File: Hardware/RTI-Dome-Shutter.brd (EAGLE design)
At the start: 80 x 71.1 mm, 42 parts, among them IC1 24AA128ST, IC5 74LVC245, IC6 74ABT245, J1 POWERPOLE_POWER45A

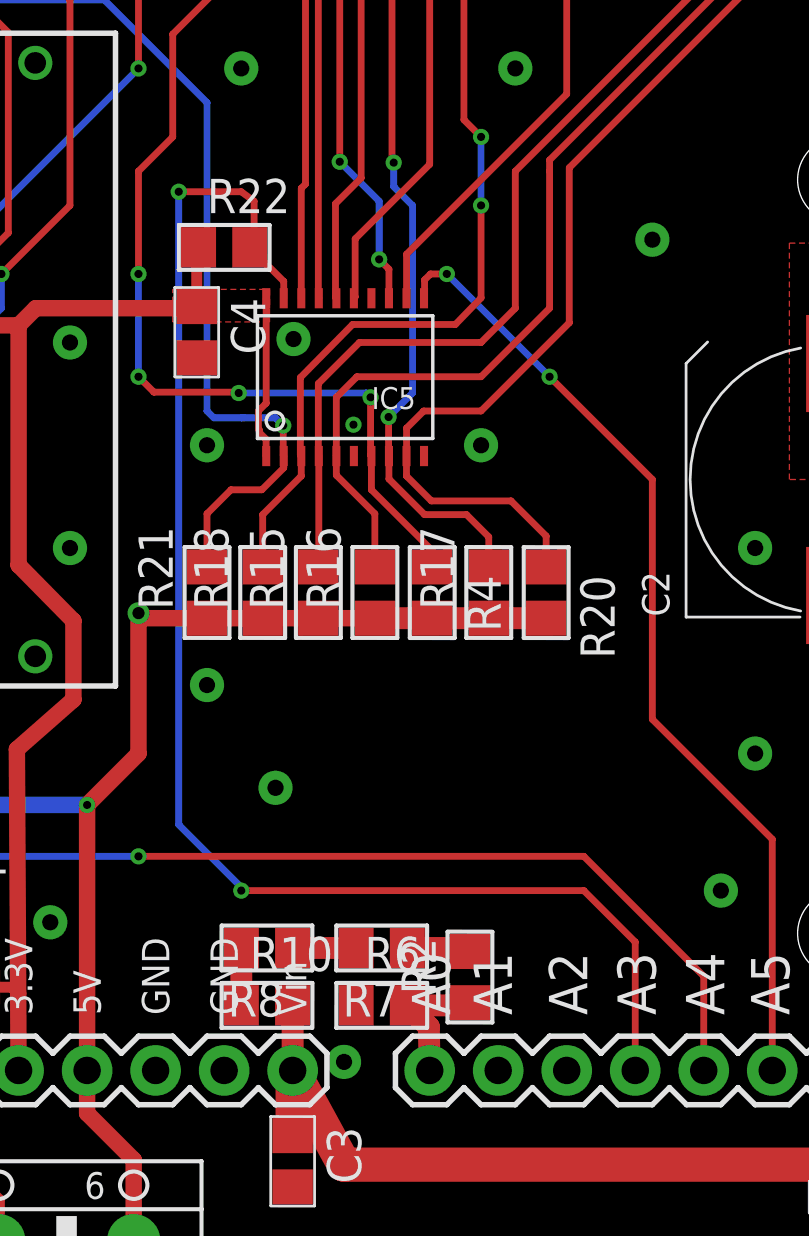
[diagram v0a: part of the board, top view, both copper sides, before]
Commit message: Added FTDI reset as it wasn't doing a proper reset on power up. Finished IP config in the plugin.
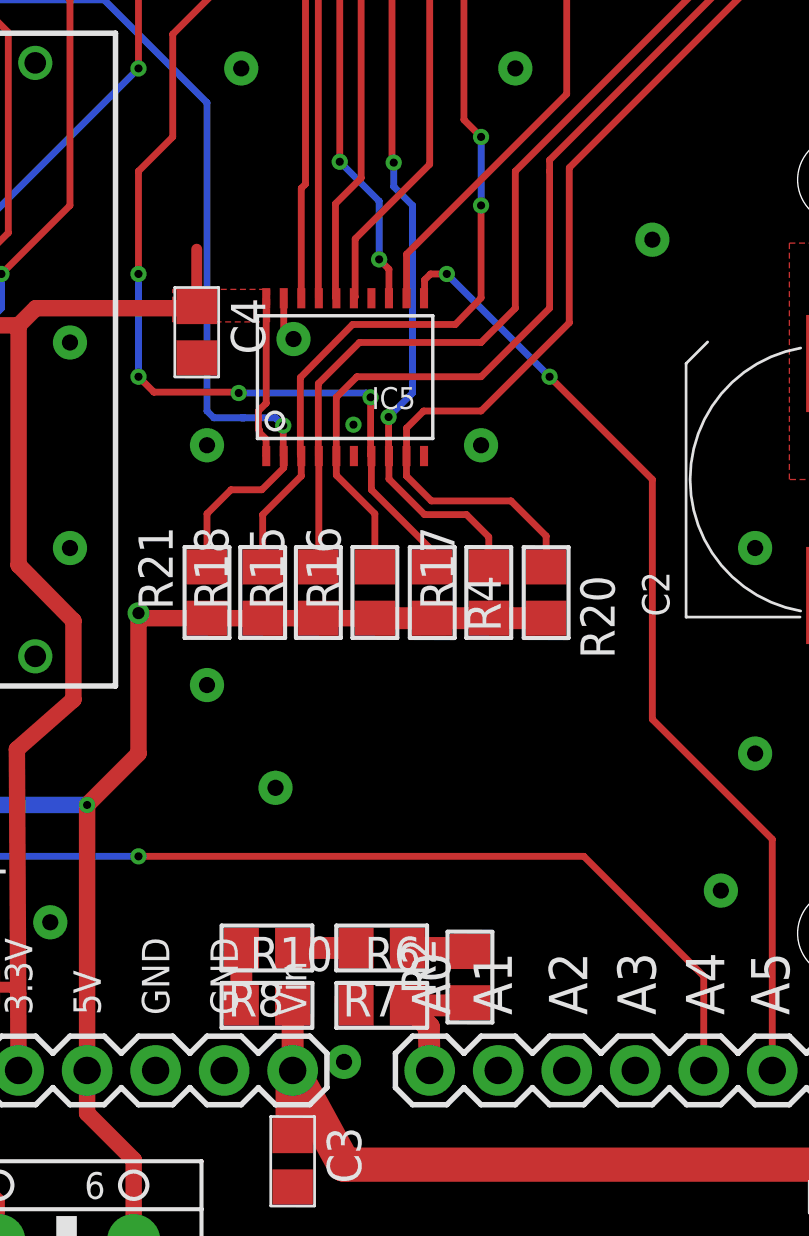
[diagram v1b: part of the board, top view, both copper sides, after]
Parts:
- removed R22: 4.7K, rti:R0805
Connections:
- removed net BUF_EN: IC5.P$19, PCB1.A3, R22.2
- net 3.3V: no longer R22.1
- net GND: now also IC5.P$19
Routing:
- net BUF_EN: track 54.1 -> 0.00 mm, vias 2 -> 0
- net GND: track 0.00 -> 1.66 mm
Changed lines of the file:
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@@
 <element name="IC5" library="rti" package="TSSOP20" value="74LVC245" x="36.83" y="36.83" rot="R90"/>
 <element name="IC6" library="rti" package="TSSOP20" value="74ABT245" x="11.43" y="19.05" rot="R180"/>
-<element name="R22" library="rti" package="R0805" value="4.7K" x="32.385" y="41.62425"/>
 <element name="J1" library="powerpoles" package="POWERPOLE_PAIR_45A" value="POWERPOLE_POWER45A" x="63.5" y="33.02" rot="R270"/>
 <element name="U$1" library="MCP120T-270I_TT" package="SOT95P237X112-3N" value="MCP120T-270I_TT" x="22.86" y="15.24">
@@
 <contactref element="J1" pad="BLACK"/>
 <contactref element="U$1" pad="3"/>
+<contactref element="IC5" pad="P$19"/>
+<wire x1="34.595" y1="39.74" x2="34.595" y2="38.58875" width="0.254" layer="1"/>
+<wire x1="34.595" y1="38.58875" x2="34.95675" y2="38.227" width="0.254" layer="1"/>
 </signal>
 <signal name="+12V" class="1">
@@
 <contactref element="IC5" pad="P$20"/>
 <contactref element="IC5" pad="P$1"/>
-<contactref element="R22" pad="1"/>
 <wire x1="33.945" y1="33.89" x2="33.94075" y2="33.89425" width="0.254" layer="1"/>
 <wire x1="33.94075" y1="33.89425" x2="33.94075" y2="34.51225" width="0.254" layer="1"/>
@@
 <wire x1="33.655" y1="35.56" x2="33.945" y2="35.85" width="0.254" layer="1"/>
 <wire x1="33.945" y1="35.85" x2="33.945" y2="39.74" width="0.254" layer="1"/>
-<wire x1="31.435" y1="41.62425" x2="31.369" y2="41.55825" width="0.4064" layer="1"/>
 <wire x1="31.369" y1="41.55825" x2="31.369" y2="39.431" width="0.4064" layer="1"/>
 <contactref element="U$1" pad="2"/>
@@
 <wire x1="3.8354" y1="63.4746" x2="5.08" y2="62.23" width="0.254" layer="1"/>
 </signal>
-<signal name="BUF_EN">
-<contactref element="IC5" pad="P$19"/>
-<contactref element="R22" pad="2"/>
-<wire x1="34.595" y1="39.74" x2="34.595" y2="40.36425" width="0.254" layer="1"/>
-<wire x1="34.595" y1="40.36425" x2="33.335" y2="41.62425" width="0.254" layer="1"/>
-<contactref element="PCB1" pad="A3"/>
-<wire x1="47.625" y1="11.1125" x2="47.625" y2="15.875" width="0.254" layer="1"/>
-<wire x1="47.625" y1="15.875" x2="45.72" y2="17.78" width="0.254" layer="1"/>
-<wire x1="45.72" y1="17.78" x2="33.02" y2="17.78" width="0.254" layer="1"/>
-<via x="33.02" y="17.78" extent="1-16" drill="0.3" diameter="0.254"/>
-<wire x1="33.02" y1="17.78" x2="33.02" y2="17.907" width="0.254" layer="16"/>
-<wire x1="33.02" y1="17.907" x2="30.70225" y2="20.22475" width="0.254" layer="16"/>
-<wire x1="30.70225" y1="20.22475" x2="30.70225" y2="43.688" width="0.254" layer="16"/>
-<via x="30.70225" y="43.688" extent="1-16" drill="0.3" diameter="0.254"/>
-<wire x1="30.70225" y1="43.688" x2="33.02" y2="43.688" width="0.254" layer="1"/>
-<wire x1="33.02" y1="43.688" x2="33.49625" y2="43.33875" width="0.254" layer="1"/>
-<wire x1="33.49625" y1="43.33875" x2="33.49625" y2="41.7855" width="0.254" layer="1"/>
-<wire x1="33.49625" y1="41.7855" x2="33.335" y2="41.62425" width="0.254" layer="1"/>
-</signal>
 <signal name="N$4">

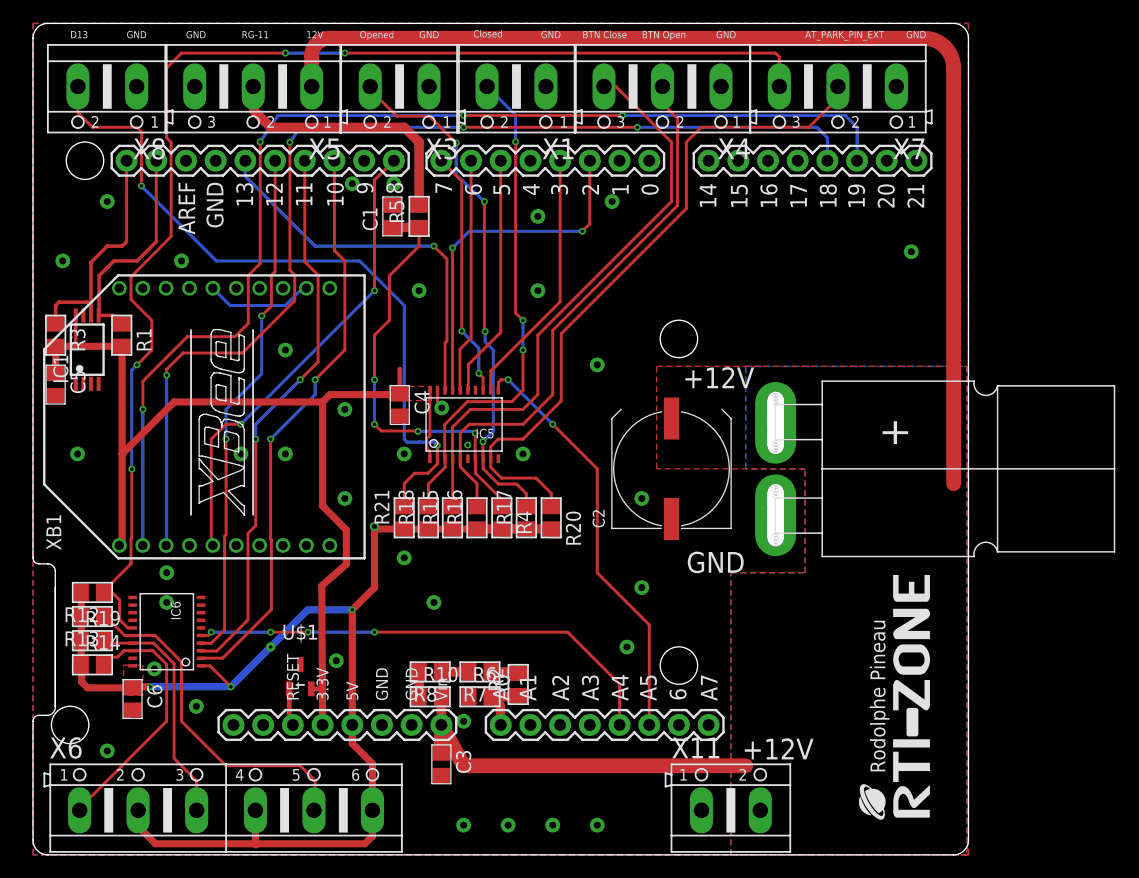
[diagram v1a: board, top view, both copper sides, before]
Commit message: Made some changes to the shutter controller to be able to control axtra linear actuator via external relay board.
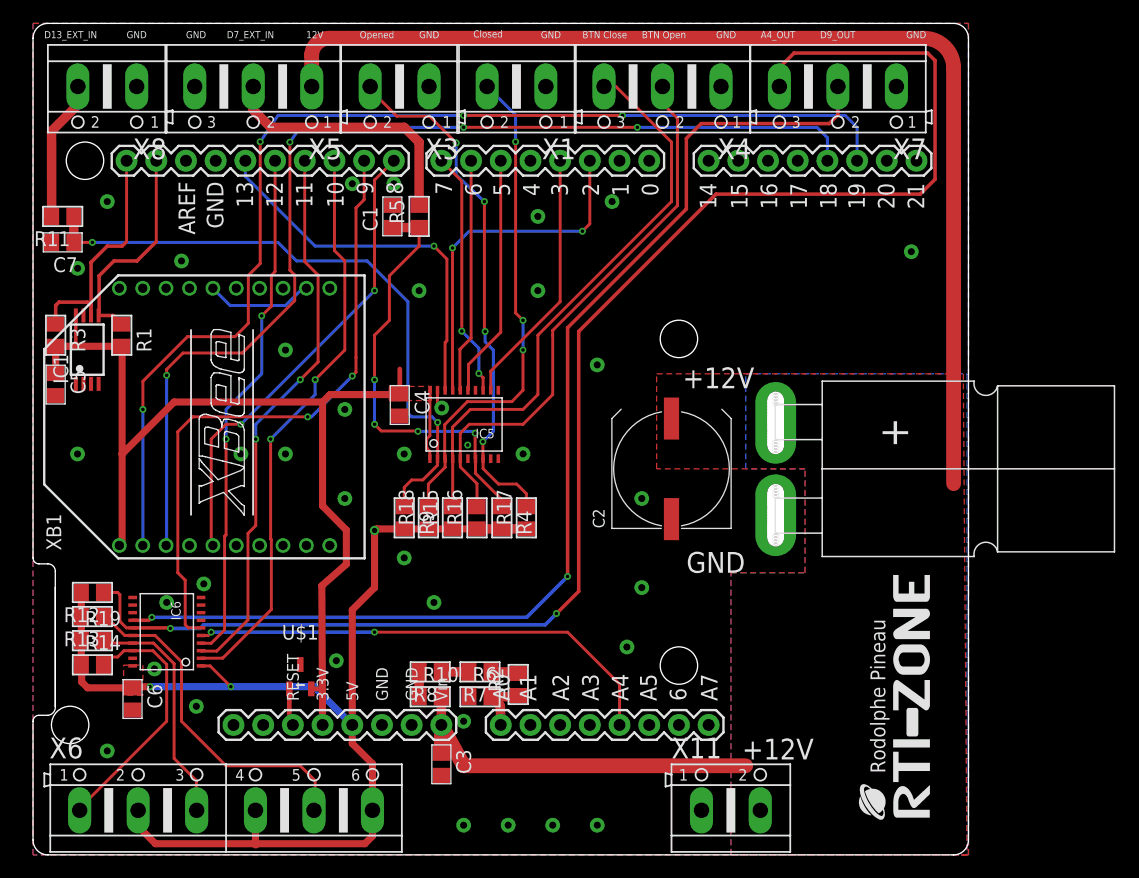
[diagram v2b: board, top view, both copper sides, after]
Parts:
- removed R20: 4.7K, rti:R0805
- added C7: 10uF, rti:C0805
- added R11: 100, rti:R0805
- turned R9 to 270 degrees
- renumbered R21 to R9
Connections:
- net AT_PARK_PIN_LOOP renamed A4_OUT
- net AT_PARK_PIN_LOOP_EXT renamed A4_OUT_5V
- net D13 renamed D13_IN
- net RG-11 renamed D7_IN
- net RG-11-IN_5V renamed D7-IN_5V
- net RG-11-IN_EXT renamed D7-IN_EXT
- removed net AT_PARK_PIN: IC5.P$11, PCB1.A5
- removed net AT_PARK_PIN_EXT: IC5.P$9, R20.1, X7.2
- new net D13_EXT_5V: C7.1, IC5.P$2, R11.1, R9.1
- new net D9_OUT: IC6.P$6, PCB1.9
- new net D9_OUT_5V: IC6.P$14, X7.2
- net D13_EXT: now also R11.2; no longer IC5.P$2, R9.2
- net GND: now also C7.2; no longer IC6.P$6
- net VCC: now also R9.2; no longer R20.2, R9.1
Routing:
- net D9_OUT_5V: track 0.00 -> 96.7 mm, vias 0 -> 2
- net AT_PARK_PIN_EXT: track 58.8 -> 0.00 mm
- net D13_EXT_5V: track 0.00 -> 54.2 mm, vias 0 -> 2
- net D9_OUT: track 0.00 -> 54.0 mm, vias 0 -> 2
- net D13_EXT: track 61.4 -> 12.0 mm, vias 2 -> 0
- net AT_PARK_PIN: track 36.1 -> 0.00 mm, vias 2 -> 0
- net A4_OUT_5V: track 109.0 -> 128.5 mm, vias 4 -> 2
- net VCC: track 105.9 -> 102.0 mm, vias 5 -> 3
- net A4_OUT: vias 4 -> 2
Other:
- board text added: "A4_OUT"
- board text added: "D13_EXT_IN"
- board text added: "D7_EXT_IN"
- board text added: "D9_OUT"
- board text removed: "AT_PARK_PIN_EXT"
- board text removed: "AT_PARK_PIN_LOOP_EXT"
- board text removed: "D13"
- board text removed: "RG-11"

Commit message: Clenup
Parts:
- U$1: value MCP120T-270I_TT -> MCP120T-315I/TT; device MCP120T-270I_TT:SOT95P237X112-3N -> MCP120T:SOT95P237X112-3N
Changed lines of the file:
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@@
 <text x="0.9525" y="69.85" size="0.6096" layer="21">D13_EXT_IN</text>
 <text x="6.50875" y="68.61175" size="0.6096" layer="22" rot="MR0">D13_EXT_IN</text>
-<text x="36.83" y="3.81" size="1.778" layer="51">Dome Shutter</text>
+<text x="35.56" y="3.4925" size="1.778" layer="21">Dome Shutter</text>
 <text x="60.6425" y="8.15975" size="1.778" layer="21">+12V</text>
 <text x="62.23" y="69.85" size="0.6096" layer="21">A4_OUT</text>
@@
 <element name="IC6" library="rti" package="TSSOP20" value="74ABT245" x="11.43" y="19.05" rot="R180"/>
 <element name="J1" library="powerpoles" package="POWERPOLE_PAIR_45A" value="POWERPOLE_POWER45A" x="63.5" y="33.02" rot="R270"/>
-<element name="U$1" library="MCP120T-270I_TT" package="SOT95P237X112-3N" value="MCP120T-270I_TT" x="22.86" y="15.24">
-<attribute name="MANUFACTURER_PART_NUMBER" value="MCP120T-270I/TT" x="22.86" y="15.24" size="1.778" layer="27" display="off"/>
+<element name="U$1" library="MCP120T" package="SOT95P237X112-3N" value="MCP120T-315I/TT" x="22.86" y="15.24">
+<attribute name="MANUFACTURER_PART_NUMBER" value="MCP120T-315I/TT" x="22.86" y="15.24" size="1.778" layer="27" display="off"/>
 <attribute name="MANUFACTURER_NAME" value="Microchip" x="22.86" y="15.24" size="1.778" layer="27" display="off"/>
-<attribute name="MOUSER_PART_NUMBER" value="579-MCP120T-270I/TT" x="22.86" y="15.24" size="1.778" layer="27" display="off"/>
+<attribute name="MOUSER_PART_NUMBER" value="579-MCP120T-315I/TT" x="22.86" y="15.24" size="1.778" layer="27" display="off"/>
 <attribute name="DESCRIPTION" value="Microcontroller Supervisory Circuit" x="22.86" y="15.24" size="1.778" layer="27" display="off"/>
 <attribute name="HEIGHT" value="mm" x="22.86" y="15.24" size="1.778" layer="27" display="off"/>
-<attribute name="MOUSER_PRICE-STOCK" value="https://www.mouser.co.uk/ProductDetail/Microchip-Technology/MCP120T-270I-TT?qs=JaP0%252BruNJH91Pwyk6aJdSA%3D%3D" x="22.86" y="15.24" size="1.778" layer="27" display="off"/>
+<attribute name="MOUSER_PRICE-STOCK" value="https://www.mouser.com/ProductDetail/Microchip-Technology/MCP120T-315I-TT/?qs=6pREnGtJ7gEI3DoW5cf%2FYQ%3D%3D" x="22.86" y="15.24" size="1.778" layer="27" display="off"/>
+<attribute name="MPN" value="MCP120T-315I/TT" x="22.86" y="15.24" size="1.778" layer="27" display="off"/>
 </element>
 <element name="R9" library="rti" package="R0805" value="4.7K" x="31.75" y="28.829" rot="R270"/>
